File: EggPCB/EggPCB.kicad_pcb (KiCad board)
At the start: 2 copper layers, 32.6 x 23.2 mm, 11 parts, among them J1 Photocell_1_V+, J2 Photocell_2_V+, J3 Photocell_1_V-, J4 Photocell_2_V-, J5 Conn_01x02_Pin, J6 Conn_01x02_Pin, J7 Photocell_1_V-, J8 GND VIA

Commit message: Work over past few days
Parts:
- removed J8: GND VIA, Connector_PinHeader_2.54mm:PinHeader_1x01_P2.54mm_Vertical
- R1, R5: footprint Resistor_SMD:R_0603_1608Metric_Pad0.98x0.95mm_HandSolder -> Resistor_THT:R_Axial_DIN0207_L6.3mm_D2.5mm_P7.62mm_Horizontal
- moved R5 3.18 mm to (107.7, 108.2)
- moved R1 2.49 mm to (107.7, 112.8)
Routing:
- net ADC2: track 25.2 -> 23.2 mm

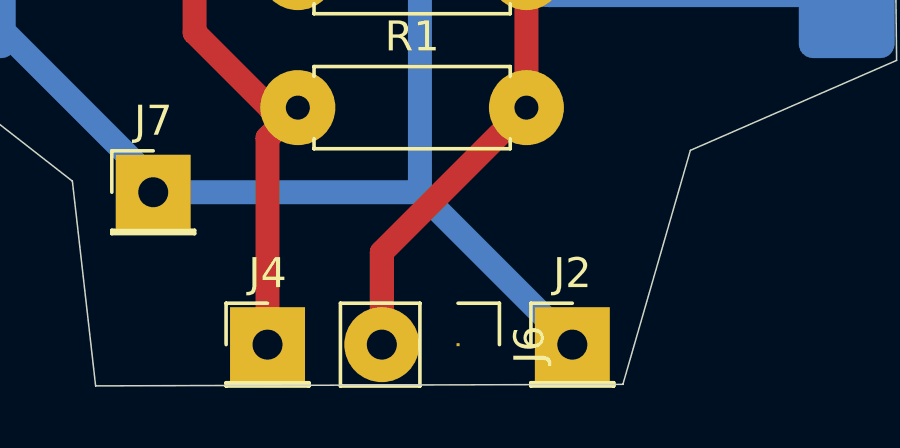
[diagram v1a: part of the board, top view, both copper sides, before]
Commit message: Updates to pcb to remove GPIO3 pin
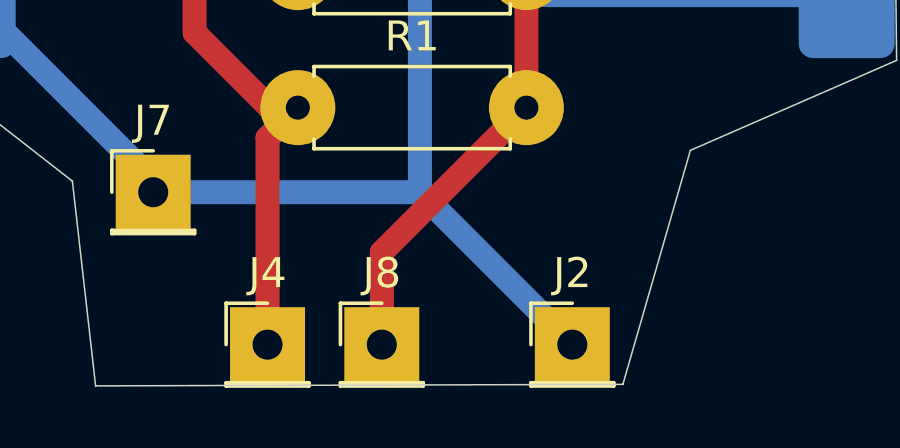
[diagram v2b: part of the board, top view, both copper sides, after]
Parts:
- removed J6: Conn_01x02_Pin, Connector_PinHeader_2.54mm:PinHeader_1x02_P2.54mm_Vertical
- added J8: GND Pin, Connector_PinHeader_2.54mm:PinHeader_1x01_P2.54mm_Vertical, F.Cu at (110.5, 120.7)
